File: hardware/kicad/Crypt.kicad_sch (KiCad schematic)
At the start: 0 parts

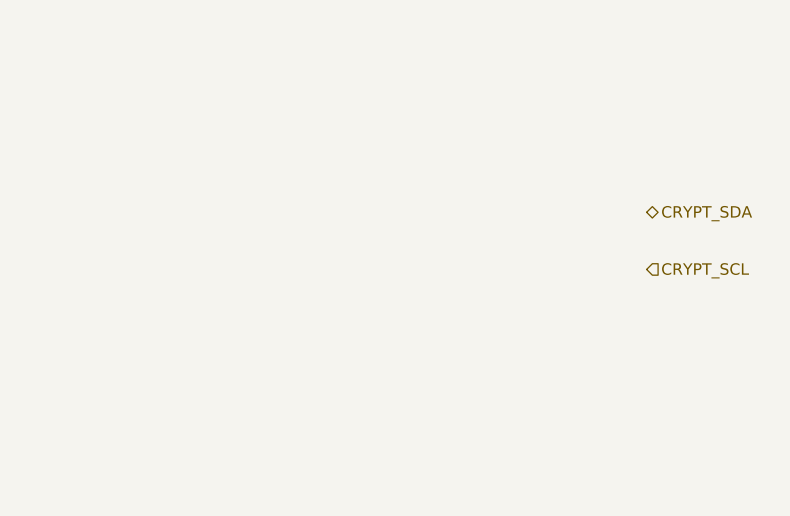
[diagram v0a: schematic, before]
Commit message: Add schematic audit, DESIGN_DECISIONS.md, and interactive website
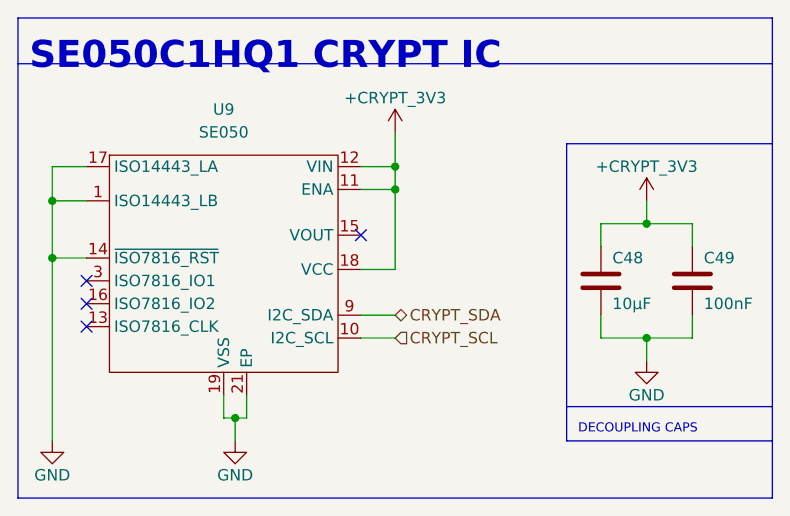
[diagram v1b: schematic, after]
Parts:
- added C48: 10μF, symbol Device:C
- added C49: 100nF, symbol Device:C
- added U9: SE050, symbol SE050:SE050
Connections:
- net CRYPT_SCL: now also U9.10 (I2C_SCL)
- net CRYPT_SDA: now also U9.9 (I2C_SDA)
- new net: U9.2 (NC), U9.20 (NC), U9.4 (NC), U9.5 (NC), U9.6 (NC), U9.7 (NC), U9.8 (NC)
- new net +CRYPT_3V3: C48.1, C49.1, U9.11 (ENA), U9.12 (VIN), U9.18 (VCC)
- new net GND: C48.2, C49.2, U9.1 (ISO14443_LB), U9.14 (~{ISO7816_RST}), U9.17 (ISO14443_LA), U9.19 (VSS), U9.21 (EP)
- no-connect marks 0 -> 4
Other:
- note added: "DECOUPLING CAPS"
- note added: "SE050C1HQ1 CRYPT IC"
